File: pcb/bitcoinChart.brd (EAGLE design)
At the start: 59.7 x 53.3 mm, 2 parts

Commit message: Added components
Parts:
- removed U$1: PINHD-1X10, adafruit:1X10-BIG
- added C1: (no value), resistor:C1206K
- added C6, C7: 10uF, basic_components:C0805K
- added D1: GREEN, SparkFun-LED:LED-1206
- added D13, D14: 1n4148, basic_components:SOD-323
- added D15, D16: MBR120, basic_components:SOD-123
- added D17: RED, basic_components:LED_0805
- added D2: RED, SparkFun-LED:LED-1206
- added R1, R2: (no value), resistor:M1206
- added R15, R16, R17, R18, R19: 10K, basic_components:R0805
- added R20: 1K, basic_components:R0805
- added S1, S2, S3: MOMENTARY-SWITCH-SPST-PTH-6.0MM-KIT, SparkFun-Switches:TACTILE_SWITCH_PTH_6.0MM_KIT
- added SV1: (no value), untitled:FE10
- added SW5, SW6: KMR2, basic_components:BTN_KMR2
- added U$42: CONN-1X6, basic_components:GHI-HEADERS_TH-1X6
- added U2: MPU-6050, MPU-6050:QFN50P400X400X95-24N
- added U7: SPX3819, basic_components:SOT-23-5
- added U8: (no value), basic_components:ESP12E-SMD
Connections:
- removed net N$13: B1.D8, U$1.8
- new net +3.3V: B1.3.3V, U2.13
- new net 3.3V: C6.1, D17.A, R15.2, R16.2, R19.2, U7.5, U8.VCC
- new net ADC: U8.ADC
- new net CH_PD: R15.1, U8.CH_PD
- new net CS0: U8.CS0
- new net GPIO0: R20.1, SW6.2, SW6.3, U8.GPIO0
- new net GPIO10: U8.GPIO10
- new net GPIO12: U8.GPIO12
- new net GPIO13: U8.GPIO13
- new net GPIO14: U8.GPIO14
- new net GPIO15: R17.2, U8.GPIO15
- new net GPIO16: U8.GPIO16
- new net GPIO2: R19.1, U8.GPIO2
- new net GPIO4: U8.GPIO4
- new net GPIO5: U8.GPIO5
- new net GPIO9: U8.GPIO9
- new net LDO_EN: R18.2, U7.3
- new net MISO: U8.MISO
- new net MOSI: U8.MOSI
- new net N$1: SV1.2
- new net N$14: C7.1, D15.1, D16.1, R18.1, U7.1
- new net N$15: D17.K, R20.2
- new net N$2: B1.A5, U2.23
- new net N$3: B1.A4, U2.24
- new net N$5: B1.D8, SV1.3
- new net RESET: D13.2, R16.1, SW5.2, SW5.3, U8.RESET
- new net RESET_5V: D13.1
- new net RXD: B1.TX, D14.2, U8.RXD0
- new net RXD_5V: D14.1, U$42.3
- new net SCLK: U8.SCLK
- new net TXD: B1.RX, U$42.2, U8.TXD0
- new net VBAT: D16.2
- new net VIN: U$42.4
- new net VLOGIC: U2.8
- net +5V: now also D15.2, SV1.5; no longer U$1.6, U$1.9
- net GND: now also B1.GND@0, B1.GND@1, B1.GND@2, C6.2, C7.2, R17.1, SV1.1, SW5.1, SW5.4, SW6.1, SW6.4, U$42.6, U2.18, U7.2, U8.GND; no longer U$1.10
- net N$4: now also SV1.10; no longer U$1.1
- net N$6: now also SV1.8; no longer U$1.3
- net N$7: now also SV1.7; no longer U$1.4
- net N$8: now also SV1.6; no longer U$1.5
- net N$9: now also SV1.4; no longer U$1.7
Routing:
- net +5V: track 77.4 -> 14.2 mm, vias 2 -> 0
- net CH_PD: track 0.00 -> 54.3 mm
- net 3.3V: track 0.00 -> 50.5 mm
- net N$14: track 0.00 -> 24.0 mm
- net RXD_5V: track 0.00 -> 13.4 mm, vias 0 -> 1
- net TXD: track 0.00 -> 12.2 mm
- net RESET: track 0.00 -> 11.1 mm, vias 0 -> 3
- net GPIO0: track 0.00 -> 9.75 mm, vias 0 -> 2
- net LDO_EN: track 0.00 -> 8.46 mm
- net RXD: track 0.00 -> 5.35 mm
- net N$9: track 5.08 -> 0.00 mm
- net N$6: track 5.08 -> 0.00 mm
- net N$13: track 5.08 -> 0.00 mm
- net N$15: track 0.00 -> 2.81 mm
- net N$8: track 6.13 -> 3.59 mm
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- added copper zone on layer 1, net GND
- removed copper zone on layer 1, net GND2

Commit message: Completed PCB
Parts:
- added C2, C4: 0.1uF, resistor:C1206K
- added C3: 10nF, resistor:C1206K
- added R3, R4, R5: 10k, resistor:M1206
- C1: value (none) -> 2.2nF
- S1, S2, S3: value MOMENTARY-SWITCH-SPST-PTH-6.0MM-KIT -> MOMENTARY-SWITCH-SPST-SMD-6.2MM-TALL; device SparkFun-Switches:TACTILE_SWITCH_PTH_6.0MM_KIT -> SparkFun-Switches:TACTILE_SWITCH_SMD_6.2MM_TALL
- moved S1 112.4 mm to (146.7, 55.2), turned to 90 degrees
- moved S3 111.7 mm to (128.9, 55.2), turned to 90 degrees
- moved S2 111.4 mm to (137.8, 55.2), turned to 90 degrees
- moved U2 83.1 mm to (118.7, 50.8)
- moved C1 74.4 mm to (118.7, 56.8), turned to 270 degrees
- moved R1 62.3 mm to (103.2, 60.0), turned to 180 degrees
- moved R2 60.2 mm to (103.2, 52.7), turned to 180 degrees
- moved D2 52.9 mm to (103.2, 55.2)
- moved D1 51.4 mm to (103.2, 57.5)
- moved U$42 0.46 mm to (108.6, 14.0)
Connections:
- removed net VLOGIC: U2.8
- new net LED_G: B1.D5, R1.1
- new net LED_R: B1.D6, R2.1
- new net N$10: C2.2, U2.10
- new net N$11: C1.2, U2.20
- new net N$12: C3.2, U2.8
- new net N$13: D1.A, R1.2
- new net N$16: D2.A, R2.2
- new net SW1: B1.D2, R3.1, S1.A2
- new net SW2: B1.D4, R4.1, S2.A2
- new net SW3: B1.D7, R5.1, S3.A2
- net +3.3V: now also C4.2
- net +5V: now also R3.2, R4.2, R5.2
- net GND: now also C1.1, C2.1, C3.1, C4.1, D1.C, D2.C, S1.B2, S2.B2, S3.B2
- net N$2: now also B1.SCL; no longer B1.A5
- net N$3: now also B1.SDA; no longer B1.A4
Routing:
- net RXD: track 5.35 -> 85.9 mm, vias 0 -> 2
- net TXD: track 12.2 -> 91.9 mm, vias 0 -> 5
- net +5V: track 14.2 -> 83.6 mm, vias 0 -> 2
- net N$5: track 0.00 -> 53.6 mm, vias 0 -> 2
- net N$9: track 0.00 -> 50.2 mm
- net LED_G: track 0.00 -> 50.1 mm, vias 0 -> 3
- net RESET: track 11.1 -> 55.8 mm, vias 3 -> 4
- net +3.3V: track 0.00 -> 44.1 mm, vias 0 -> 4
- net LED_R: track 0.00 -> 41.9 mm, vias 0 -> 3
- net N$8: track 3.59 -> 41.8 mm
- net N$7: track 3.59 -> 38.3 mm, vias 0 -> 1
- net N$6: track 0.00 -> 33.2 mm
- net GPIO0: track 9.75 -> 32.8 mm, vias 2 -> 4
- net GPIO2: track 2.23 -> 21.2 mm
- net SW3: track 0.00 -> 17.7 mm
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
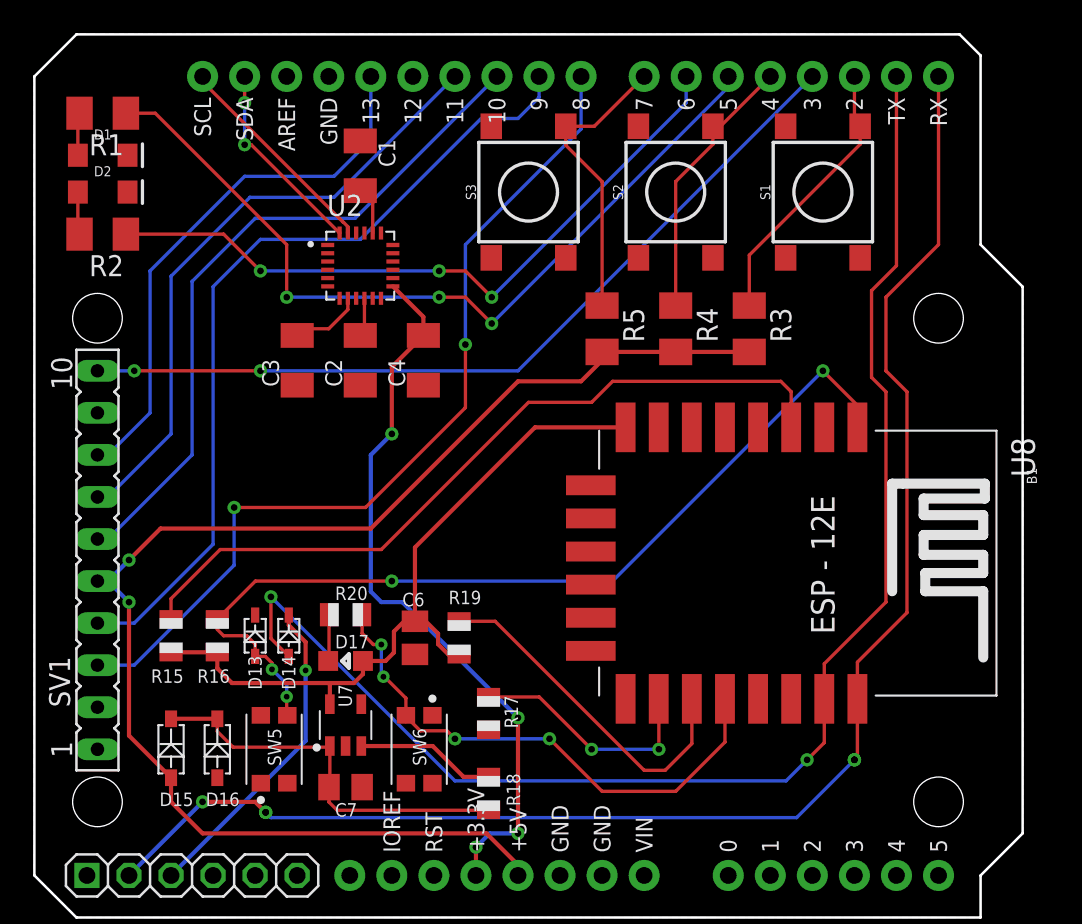
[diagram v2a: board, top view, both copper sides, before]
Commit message: Changed LED package, removed routing over antenna
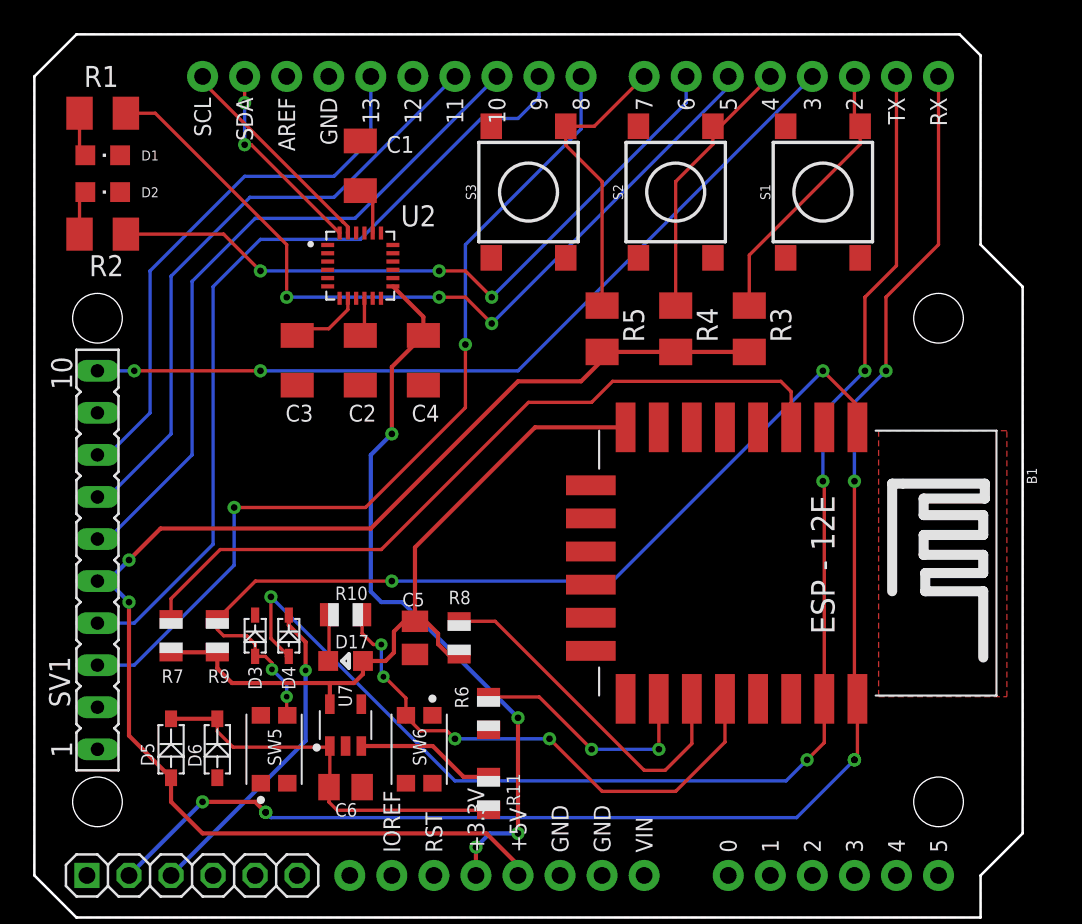
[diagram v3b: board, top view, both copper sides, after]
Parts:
- removed C7: 10uF, basic_components:C0805K
- added C5: 10uF, basic_components:C0805K
- D1, D2: device SparkFun-LED:LED-1206 -> led:CHIPLED_0805
- R1: value (none) -> 150
- R2: value (none) -> 160
- moved C6 9.94 mm to (117.9, 19.3), turned to 0 degrees
- turned D1 to 270 degrees
- turned D2 to 270 degrees
- renumbered D13 to D3, D14 to D4, D15 to D5, D16 to D6, R15 to R7, R16 to R9, R17 to R6, R18 to R11, R19 to R8, R20 to R10
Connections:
- net 3.3V: now also C5.1; no longer C6.1
- net GND: now also C5.2; no longer C7.2
- net N$14: now also C6.1; no longer C7.1
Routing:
- net TXD: track 91.9 -> 91.0 mm, vias 5 -> 7
- net RXD: track 85.9 -> 85.3 mm, vias 2 -> 4
- added copper zone on layer 1, net ANTENNA

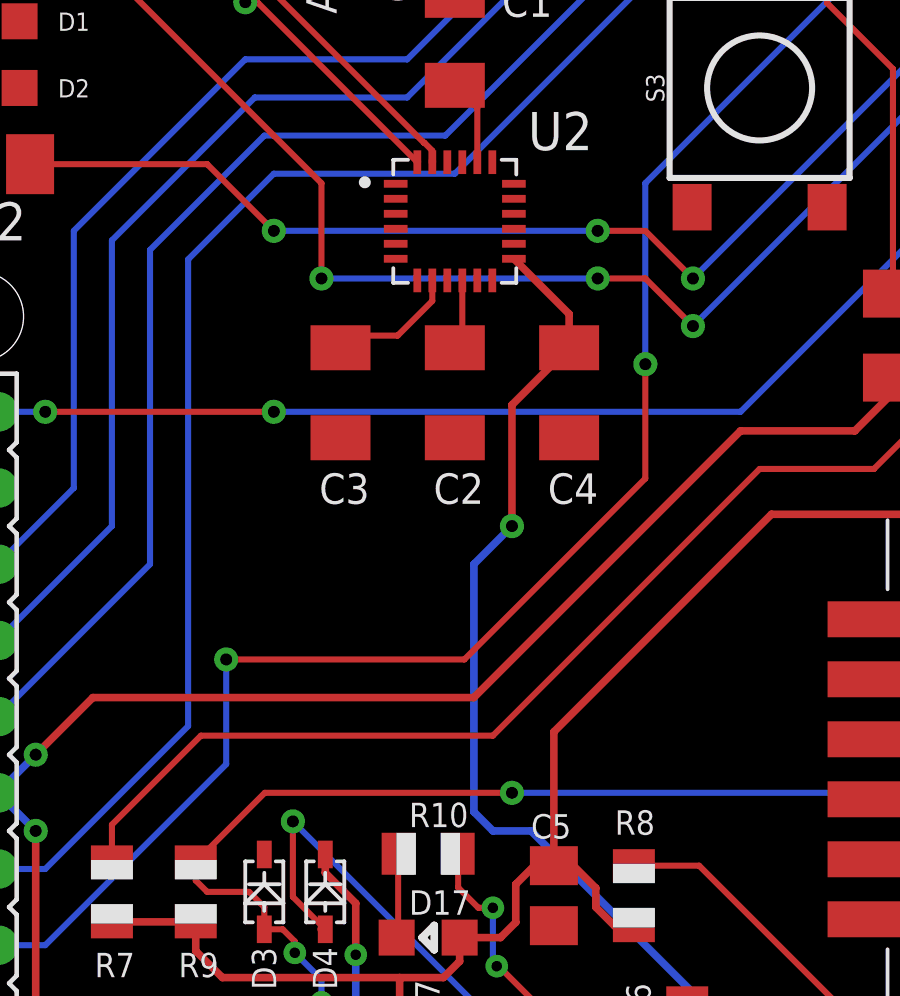
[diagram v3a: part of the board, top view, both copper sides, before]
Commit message: Picture, connected some pins on MPU6050
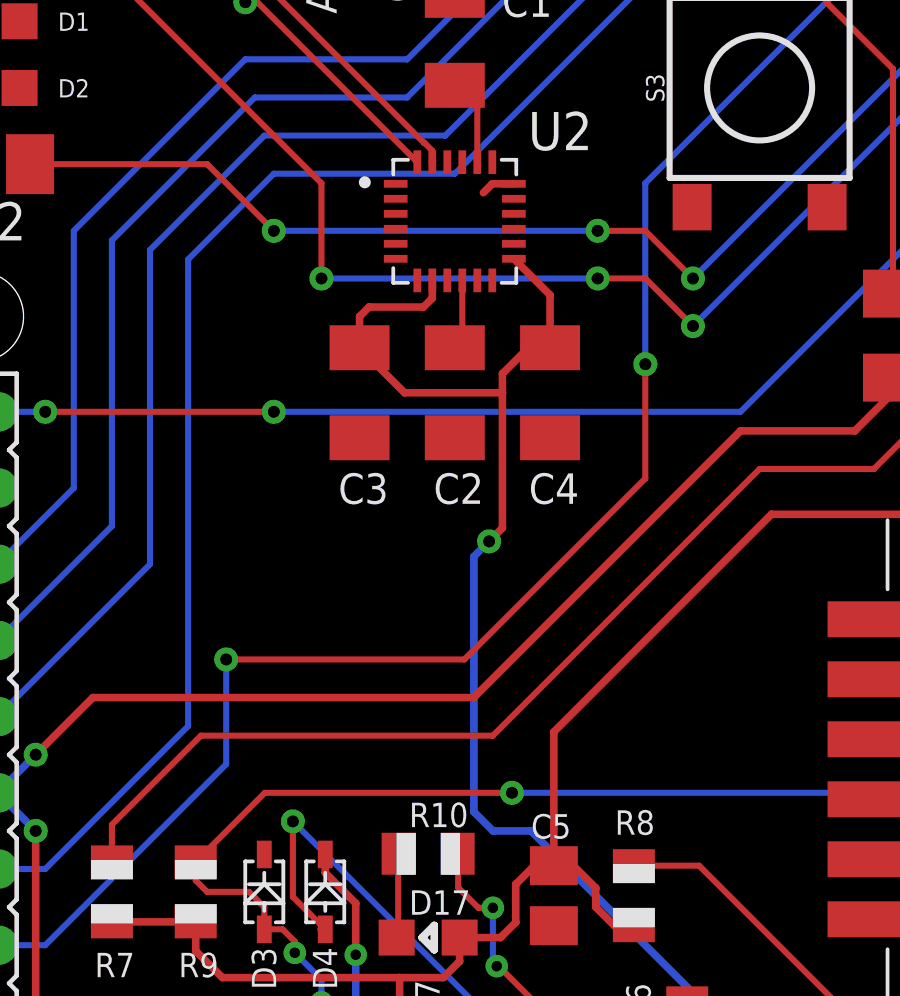
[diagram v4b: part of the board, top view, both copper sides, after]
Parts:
- moved C4 0.64 mm to (121.9, 45.1)
- moved C3 0.63 mm to (115.6, 45.1)
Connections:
- removed net N$12: C3.2, U2.8
- net +3.3V: now also C3.2, U2.8
- net GND: now also U2.1, U2.11, U2.9
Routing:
- net +3.3V: track 44.1 -> 53.8 mm
- net N$12: track 4.22 -> 0.00 mm
- net GND: track 0.00 -> 1.14 mm
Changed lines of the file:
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@@
 </class>
 <class number="1" name="test" width="0.1524" drill="0.4">
-<clearance class="1" value="0.3"/>
 </class>
 <class number="2" name="3v" width="0.1524" drill="0.3">
@@
 <attribute name="VALUE" x="120.845" y="43.485" size="1.016" layer="27" rot="R90"/>
 </element>
-<element name="C3" library="resistor" library_urn="urn:adsk.eagle:library:348" package="C1206K" package3d_urn="urn:adsk.eagle:package:23682/2" value="10nF" x="114.935" y="45.085" smashed="yes" rot="R90">
-<attribute name="NAME" x="115.9" y="42.3975" size="1.016" layer="25" rot="R180"/>
-<attribute name="VALUE" x="117.035" y="43.485" size="1.016" layer="27" rot="R90"/>
-</element>
-<element name="C4" library="resistor" library_urn="urn:adsk.eagle:library:348" package="C1206K" package3d_urn="urn:adsk.eagle:package:23682/2" value="0.1uF" x="122.555" y="45.085" smashed="yes" rot="R90">
-<attribute name="NAME" x="123.52" y="42.3975" size="1.016" layer="25" rot="R180"/>
-<attribute name="VALUE" x="124.655" y="43.485" size="1.016" layer="27" rot="R90"/>
+<element name="C3" library="resistor" library_urn="urn:adsk.eagle:library:348" package="C1206K" package3d_urn="urn:adsk.eagle:package:23682/2" value="10nF" x="115.57" y="45.085" smashed="yes" rot="R90">
+<attribute name="NAME" x="116.535" y="42.3975" size="1.016" layer="25" rot="R180"/>
+<attribute name="VALUE" x="117.67" y="43.485" size="1.016" layer="27" rot="R90"/>
+</element>
+<element name="C4" library="resistor" library_urn="urn:adsk.eagle:library:348" package="C1206K" package3d_urn="urn:adsk.eagle:package:23682/2" value="0.1uF" x="121.92" y="45.085" smashed="yes" rot="R90">
+<attribute name="NAME" x="122.885" y="42.3975" size="1.016" layer="25" rot="R180"/>
+<attribute name="VALUE" x="124.02" y="43.485" size="1.016" layer="27" rot="R90"/>
 </element>
 <element name="R3" library="resistor" library_urn="urn:adsk.eagle:library:348" package="M1206" package3d_urn="urn:adsk.eagle:package:23566/1" value="10k" x="142.24" y="46.99" smashed="yes" rot="R270">
@@
 <contactref element="U8" pad="GND"/>
 <contactref element="U$42" pad="6"/>
-<polygon width="0.1524" layer="1">
+<polygon width="0.1524" layer="1" isolate="0.254">
 <vertex x="99.06" y="62.23"/>
 <vertex x="99.06" y="13.97"/>
@@
 <contactref element="S2" pad="B2"/>
 <contactref element="S1" pad="B2"/>
+<contactref element="U2" pad="1"/>
+<contactref element="U2" pad="9"/>
+<contactref element="U2" pad="11"/>
+<wire x1="120.715" y1="52.05" x2="119.995" y2="52.05" width="0.254" layer="1"/>
+<wire x1="119.995" y1="52.05" x2="119.6975" y2="51.7525" width="0.254" layer="1"/>
 </signal>
 <signal name="+5V" class="1">
@@
 <wire x1="121.285" y1="30.48" x2="120.015" y2="30.48" width="0.254" layer="16"/>
 <wire x1="120.015" y1="30.48" x2="119.38" y2="31.115" width="0.254" layer="16"/>
-<wire x1="119.38" y1="31.115" x2="119.38" y2="39.37" width="0.254" layer="16"/>
-<wire x1="119.38" y1="39.37" x2="120.65" y2="40.64" width="0.254" layer="16"/>
-<via x="120.65" y="40.64" extent="1-16" drill="0.4"/>
-<wire x1="120.65" y1="40.64" x2="120.65" y2="44.68" width="0.254" layer="1"/>
-<wire x1="120.65" y1="44.68" x2="122.555" y2="46.585" width="0.254" layer="1"/>
-<wire x1="120.715" y1="49.55" x2="122.555" y2="47.71" width="0.254" layer="1"/>
-<wire x1="122.555" y1="47.71" x2="122.555" y2="46.585" width="0.254" layer="1"/>
+<wire x1="119.38" y1="31.115" x2="119.38" y2="39.624" width="0.254" layer="16"/>
+<wire x1="119.38" y1="39.624" x2="119.888" y2="40.132" width="0.254" layer="16"/>
+<via x="119.888" y="40.132" extent="1-16" drill="0.4"/>
+<wire x1="120.3325" y1="45.085" x2="120.3325" y2="40.5765" width="0.254" layer="1"/>
+<wire x1="119.888" y1="40.132" x2="120.3325" y2="40.5765" width="0.254" layer="1"/>
+<wire x1="120.715" y1="49.55" x2="121.92" y2="48.345" width="0.254" layer="1"/>
+<wire x1="121.92" y1="48.345" x2="121.92" y2="46.585" width="0.254" layer="1"/>
+<contactref element="U2" pad="8"/>
+<contactref element="C3" pad="2"/>
+<wire x1="115.57" y1="46.585" x2="115.57" y2="47.625" width="0.254" layer="1"/>
+<wire x1="115.57" y1="47.625" x2="115.8875" y2="47.9425" width="0.254" layer="1"/>
+<wire x1="117.70045" y1="47.9425" x2="115.8875" y2="47.9425" width="0.254" layer="1"/>
+<wire x1="117.995" y1="48.83" x2="117.995" y2="48.23705" width="0.254" layer="1"/>
+<wire x1="117.995" y1="48.23705" x2="117.70045" y2="47.9425" width="0.254" layer="1"/>
+<wire x1="120.3325" y1="45.085" x2="120.3325" y2="45.72" width="0.254" layer="1"/>
+<wire x1="120.3325" y1="45.72" x2="121.285" y2="46.6725" width="0.254" layer="1"/>
+<wire x1="121.285" y1="46.6725" x2="121.3725" y2="46.585" width="0.2032" layer="1"/>
+<wire x1="121.3725" y1="46.585" x2="121.92" y2="46.585" width="0.254" layer="1"/>
+<wire x1="117.07" y1="45.085" x2="115.57" y2="46.585" width="0.254" layer="1"/>
+<wire x1="120.3325" y1="45.085" x2="117.07" y2="45.085" width="0.254" layer="1"/>
 </signal>
 <signal name="N$5">
@@
 <wire x1="119.495" y1="54.5825" x2="118.745" y2="55.3325" width="0.2032" layer="1"/>
 </signal>
-<signal name="N$12">
-<contactref element="U2" pad="8"/>
-<contactref element="C3" pad="2"/>
-<wire x1="117.995" y1="48.83" x2="117.995" y2="48.145" width="0.2032" layer="1"/>
-<wire x1="117.995" y1="48.145" x2="116.84" y2="46.99" width="0.2032" layer="1"/>
-<wire x1="116.84" y1="46.99" x2="114.935" y2="46.99" width="0.2032" layer="1"/>
-<wire x1="114.935" y1="46.99" x2="114.935" y2="46.585" width="0" layer="19" extent="1-1"/>
-</signal>
 <signal name="N$13">
